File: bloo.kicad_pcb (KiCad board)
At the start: 2 copper layers, 90 x 96 mm, 97 parts, among them J5 SWD_Header, M1 M1_Conn_Alt, M2 M2_Conn_Alt, Q0 TEFT4300, Q1 TEFT4300, Q10 Q_NMOS_GSD, Q11 Q_NMOS_GSD, Q12 Q_NMOS_GSD, Q2 TEFT4300, Q3 TEFT4300, Q9 Q_NMOS_GSD, SW1 SW, SW2 SW, SW3 SW, U1 YAAJ_BluePill_SWD_Breakout, U2 L293D, U3 LM1085-5.0, U4 NCP161ASN330T1G, U5 BC832, Y1 ABS07-32.768KHZ-T

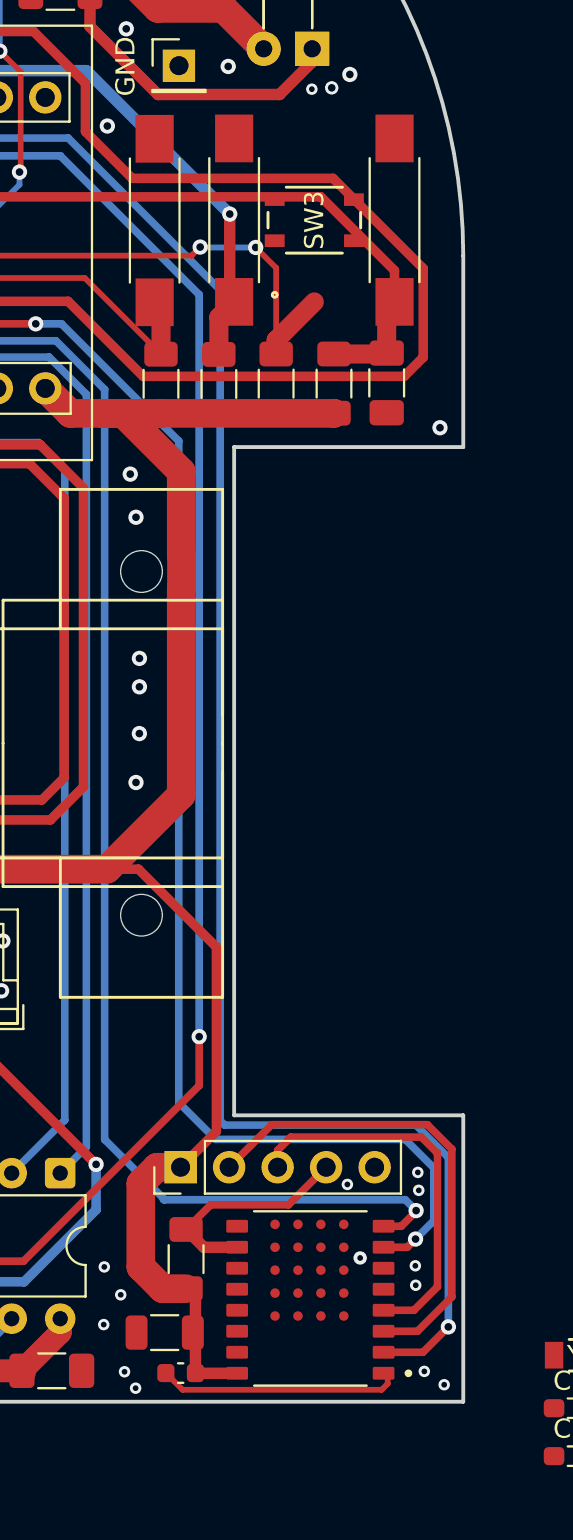
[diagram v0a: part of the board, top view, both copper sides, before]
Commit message: updated buttons in pcb
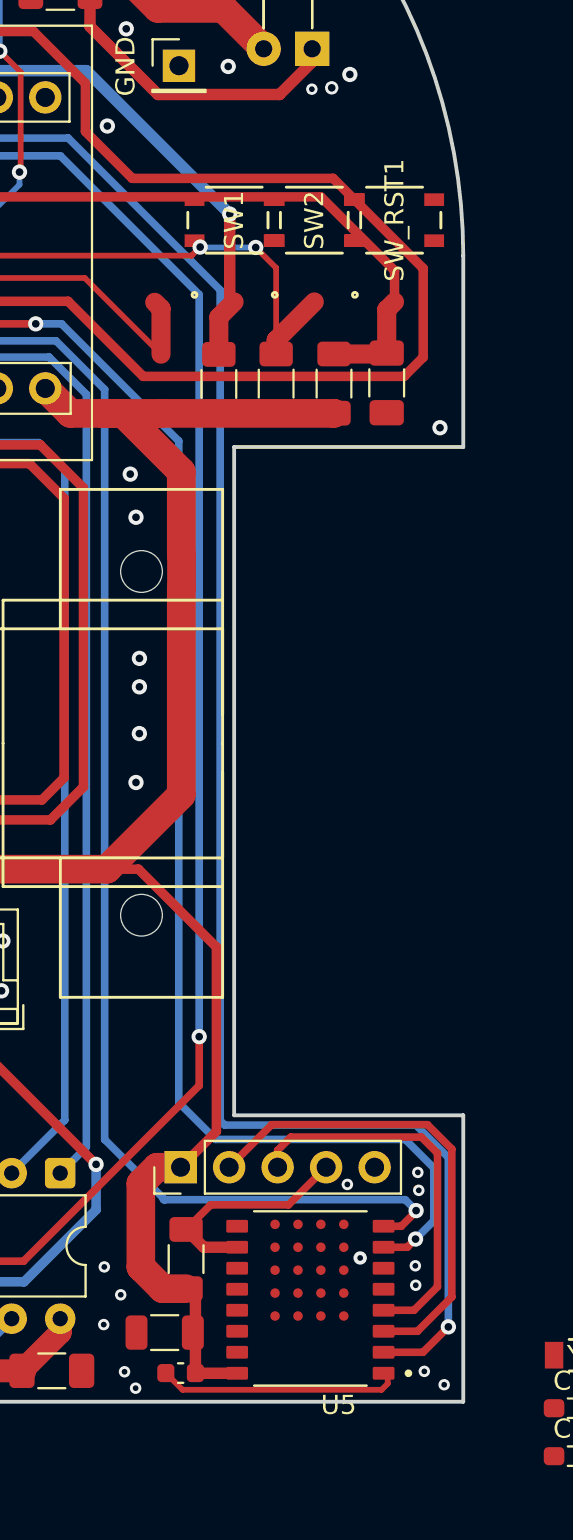
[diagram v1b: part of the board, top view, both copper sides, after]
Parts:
- removed R11: 47K, Resistor_SMD:R_1206_3216Metric_Pad1.30x1.75mm_HandSolder
- removed the SW1 at (283.3, 73.2)
- SW1: renamed from SW2; footprint Button_Switch_SMD:SW_SPST_REED_CT05-XXXX-G1 -> MM_Library:SW4_SKRPABE010_ALPS
- SW_RST1: footprint Button_Switch_SMD:SW_SPST_REED_CT05-XXXX-G1 -> MM_Library:SW4_SKRPABE010_ALPS
- U5: footprint custom_foot:XCVR_BC832 -> MM_Library:XCVR_BC832
- renumbered SW3 to SW2
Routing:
- net BUTTON: track 60.1 -> 26.8 mm, vias 2 -> 1
- net BLE_SPI_MISO: track 0.00 -> 33.3 mm, vias 0 -> 1

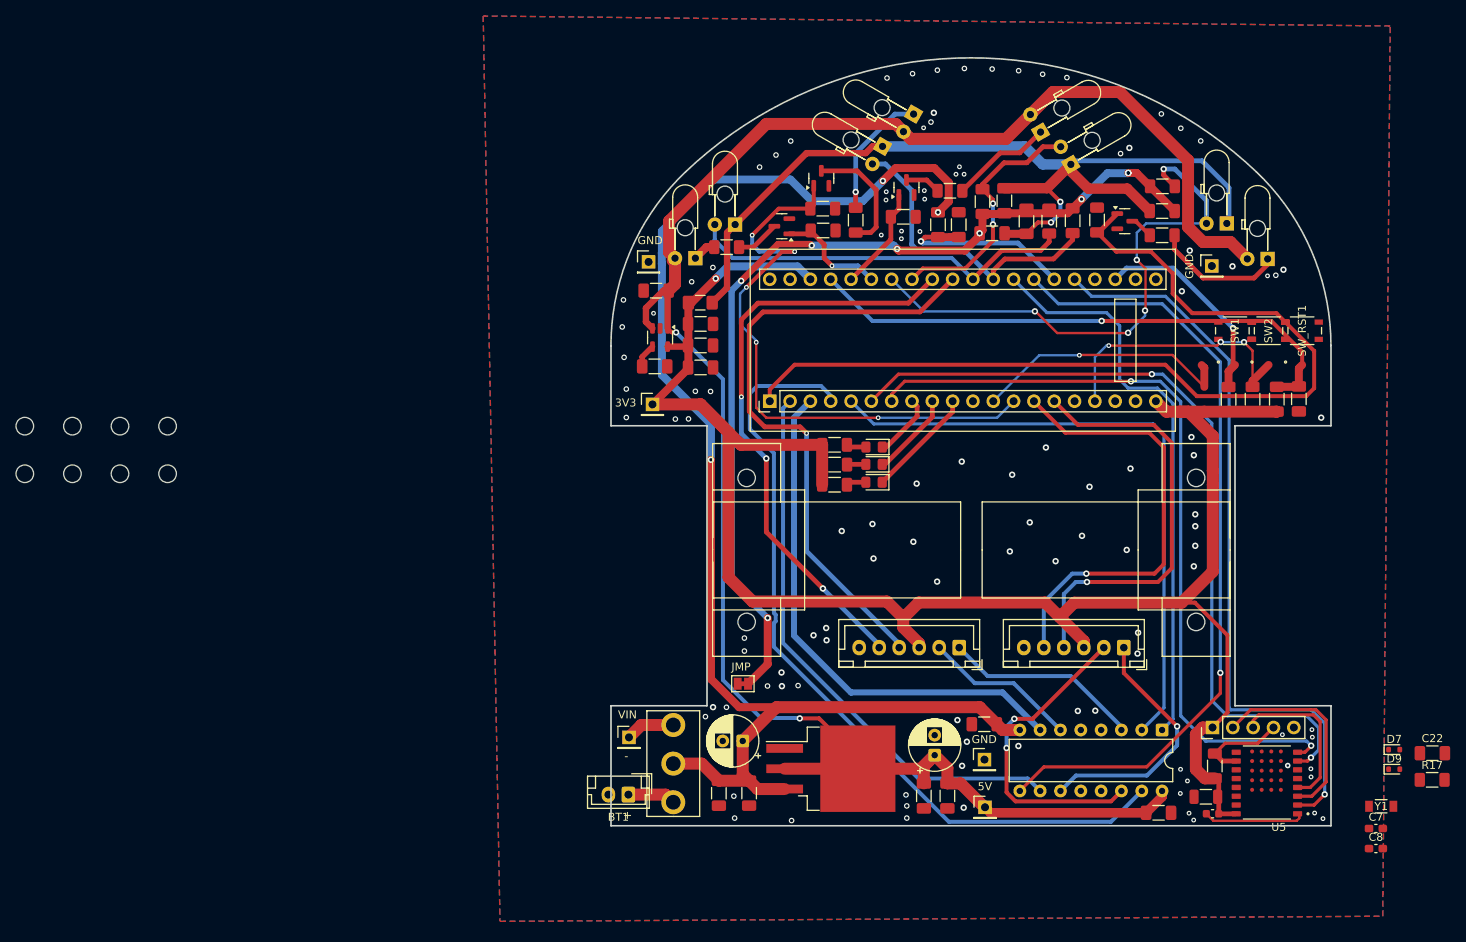
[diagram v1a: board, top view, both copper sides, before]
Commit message: started new part placement and routing
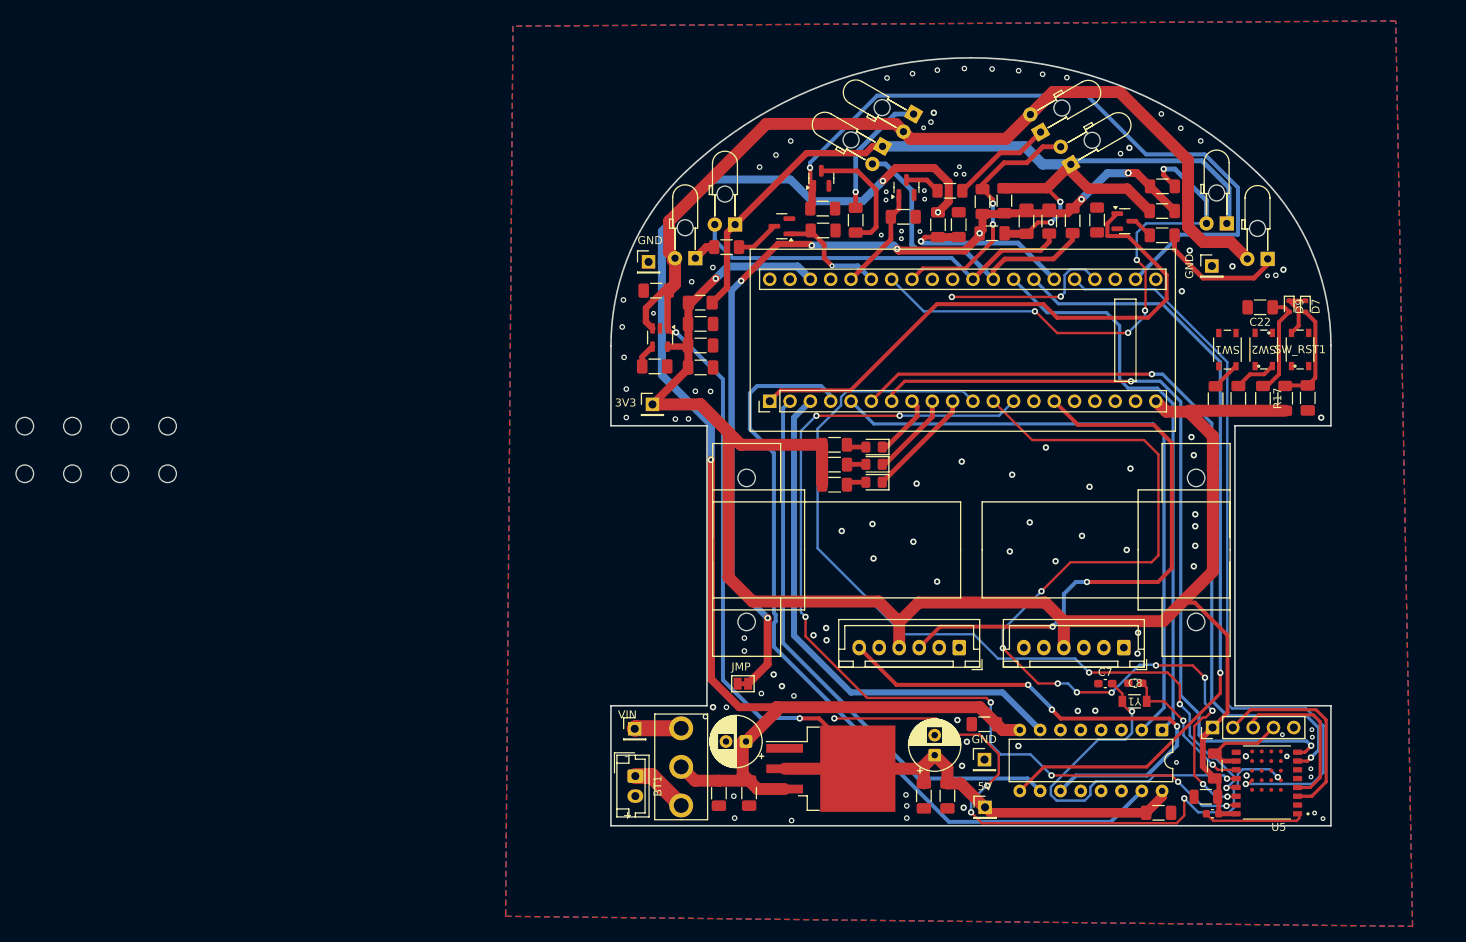
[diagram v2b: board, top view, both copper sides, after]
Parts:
- moved C22 59.8 mm to (290.6, 70.3), turned to 180 degrees
- moved D9 59.3 mm to (294.3, 70.2), turned to -90 degrees
- moved D7 56.5 mm to (296.3, 70.2), turned to -90 degrees
- moved R17 52.2 mm to (291.0, 81.7), turned to -90 degrees
- moved C7 38.4 mm to (271.3, 117.3)
- moved C8 36.5 mm to (275.0, 117.3)
- moved Y1 33.5 mm to (274.9, 119.5), turned to 180 degrees
- moved SW1 2.55 mm to (286.6, 75.6), turned to 180 degrees
- moved BT1 2.48 mm to (212.6, 128.9), turned to -90 degrees
- moved SW2 2.43 mm to (291.1, 75.6), turned to 180 degrees
- moved SW_RST1 2.36 mm to (295.6, 75.6), turned to 0 degrees
- moved R9 1.78 mm to (287.9, 81.7)
- moved R24 1.62 mm to (285.1, 81.7)
- moved TP1 1.29 mm to (212.5, 123.0)
- moved C19 1.12 mm to (296.6, 81.6), turned to 90 degrees
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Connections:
- U5 pad 13: unconnected-(U5-P02/AIN0-Pad13) -> BLE_SPI_SCK
- U5 pad 14: unconnected-(U5-P27/SCL-Pad14) -> BLE_SPI_MISO
- U5 pad 15: unconnected-(U5-P26/SDA-Pad15) -> BLE_SPI_MOSI
- U5 pad A5: BLE_SPI_SCK -> unconnected-(U5-P08-PadA5)
- U5 pad C5: BLE_SPI_MISO -> unconnected-(U5-P09-PadC5)
- U5 pad D5: BLE_SPI_MOSI -> unconnected-(U5-P10-PadD5)
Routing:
- net BLE_SPI_MOSI: track 0.00 -> 119.8 mm, vias 0 -> 7
- net BLE_SPI_SCK: track 0.00 -> 107.3 mm, vias 0 -> 3
- net BLE_LED: track 0.00 -> 99.8 mm, vias 0 -> 7
- net M1_ENC_A: track 78.4 -> 0.00 mm, vias 1 -> 0
- net BLE_SPI_MISO: track 33.3 -> 111.4 mm, vias 1 -> 10
- net M1_ENC_B: track 74.3 -> 0.00 mm, vias 3 -> 0
- net RST: track 70.0 -> 13.0 mm, vias 1 -> 0
- net M2_ENC_B: track 55.9 -> 0.00 mm, vias 1 -> 0
- net Net-(U5-P01/XL2): track 0.00 -> 46.8 mm, vias 0 -> 2
- net EMIT_1: track 115.7 -> 72.1 mm
- net M2_OUT_2: track 39.8 -> 0.00 mm, vias 2 -> 0
- net M2_OUT_1: track 31.9 -> 63.2 mm, vias 1 -> 3
- net BUTTON_2: track 34.5 -> 5.28 mm, vias 3 -> 0
- net M1_OUT_1: track 24.8 -> 0.00 mm
- net BUTTON: track 26.8 -> 3.59 mm, vias 1 -> 0
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
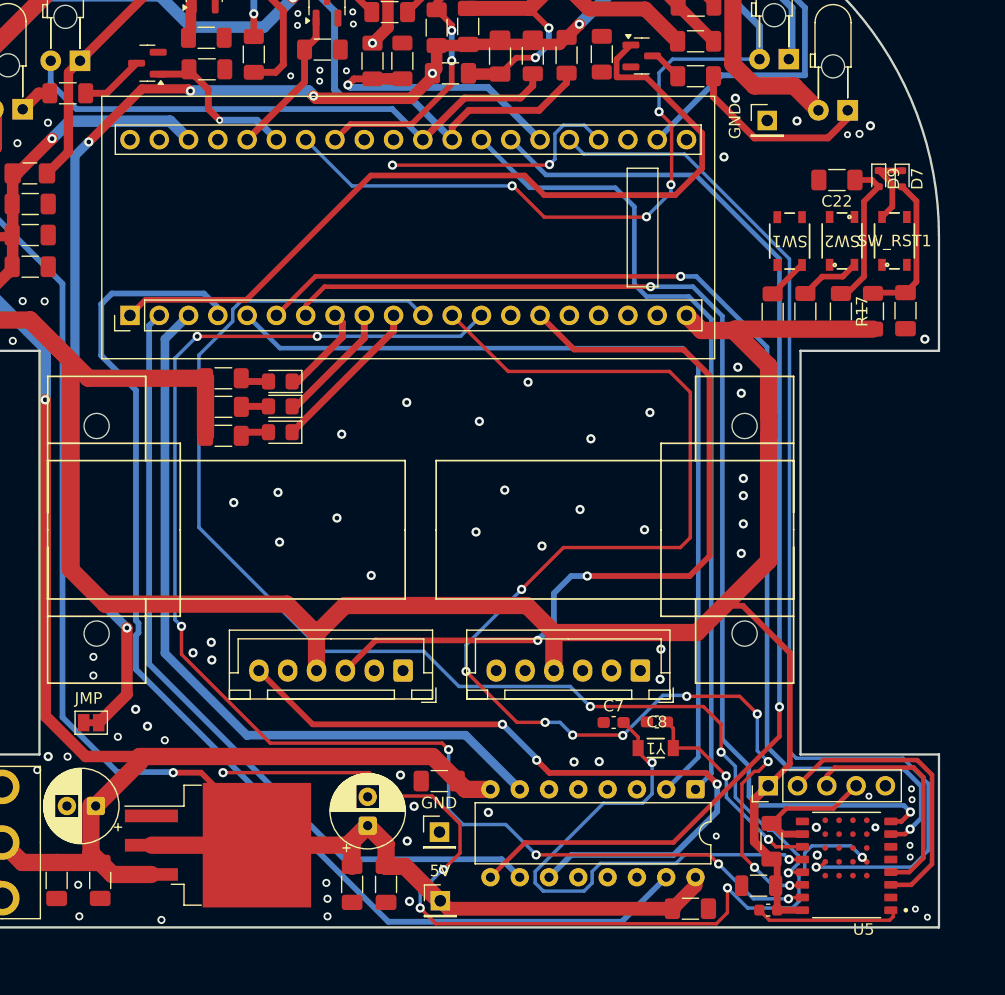
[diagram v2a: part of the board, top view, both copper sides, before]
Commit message: finished rerouting + no more DRC errors
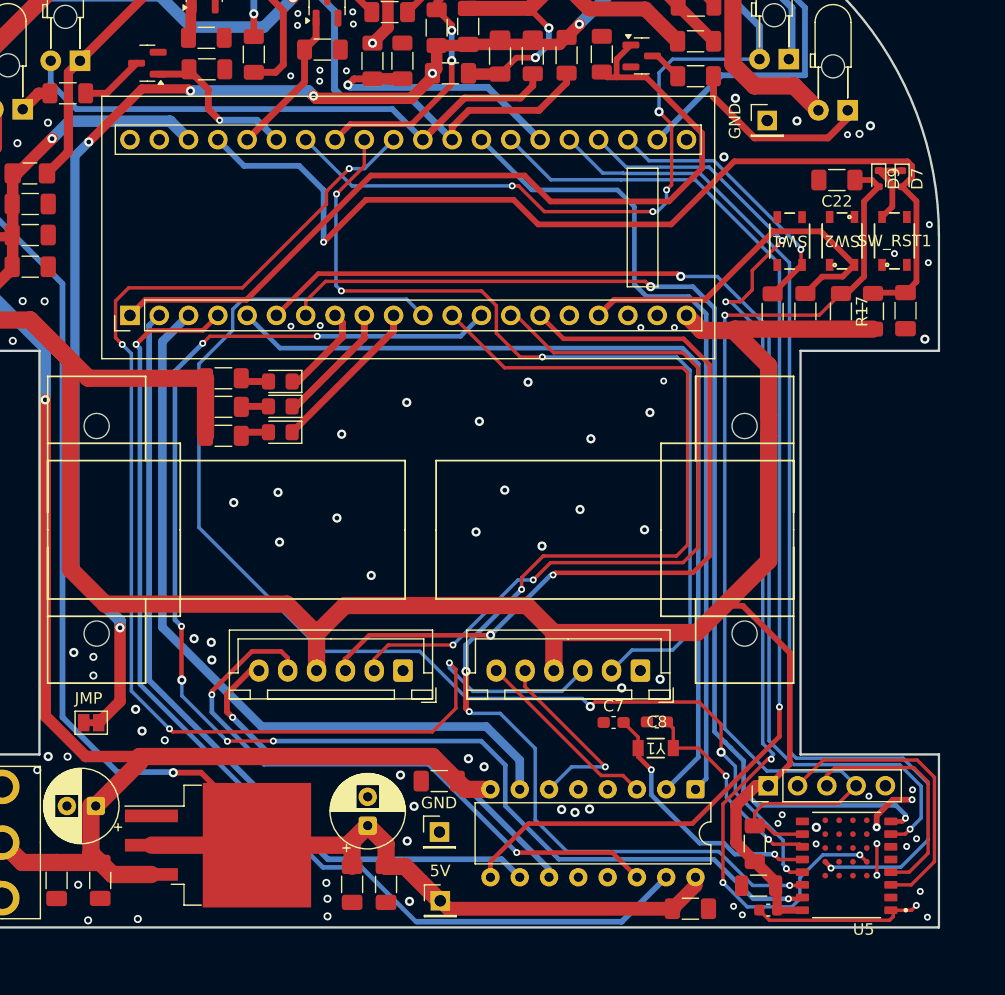
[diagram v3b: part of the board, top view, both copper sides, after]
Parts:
- moved R10 1.47 mm to (283.5, 127.8)
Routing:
- net M1_ENC_A: track 0.00 -> 113.1 mm, vias 0 -> 4
- net M1_ENC_B: track 0.00 -> 79.7 mm, vias 0 -> 3
- net RST: track 13.0 -> 86.5 mm, vias 0 -> 1
- net M2_ENC_B: track 0.00 -> 66.8 mm, vias 0 -> 2
- net BT_RESET: track 25.0 -> 88.7 mm, vias 0 -> 1
- net M2_OUT_2: track 0.00 -> 53.9 mm, vias 0 -> 2
- net BUTTON_2: track 5.28 -> 31.7 mm
- net M2_OUT_1: track 63.2 -> 39.4 mm, vias 3 -> 1
- net Net-(U5-P01/XL2): track 46.8 -> 23.1 mm
- net BUTTON: track 3.59 -> 23.9 mm, vias 0 -> 1
- net M1_OUT_2: track 0.00 -> 16.9 mm, vias 0 -> 1
- net M1_OUT_1: track 0.00 -> 16.5 mm
- net GND: track 12.8 -> 22.6 mm, vias 109 -> 119
- net M2_BACK: track 101.4 -> 93.5 mm, vias 0 -> 1
- net BLE_SPI_MISO: track 111.4 -> 105.5 mm, vias 10 -> 4
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
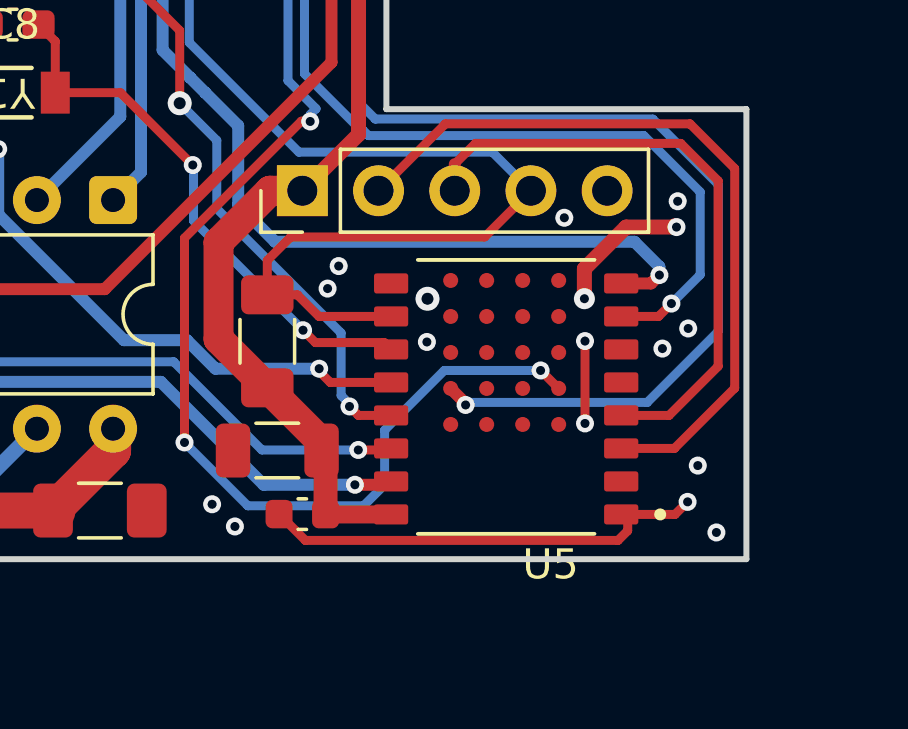
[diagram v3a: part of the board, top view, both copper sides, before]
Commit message: rerouted LED/State to edge pins on BLE
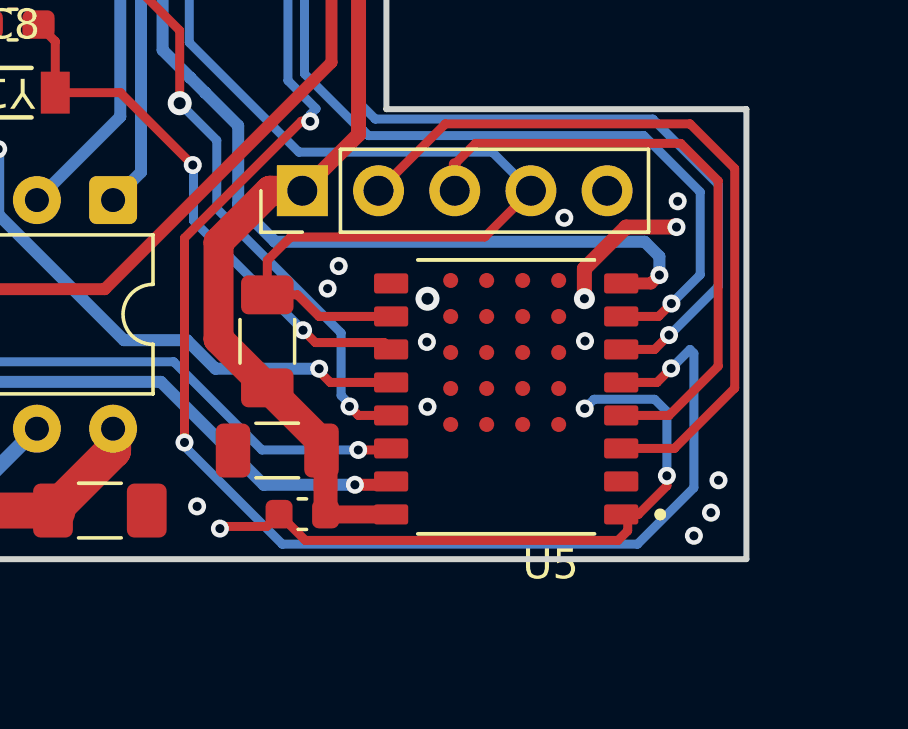
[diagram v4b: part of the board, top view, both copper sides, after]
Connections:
- U5 pad 5: unconnected-(U5-P18/LED-Pad5) -> BLE_LED
- U5 pad 6: unconnected-(U5-P13/BUTTON-Pad6) -> BLE_STATE
- U5 pad A2: BLE_LED -> unconnected-(U5-P17-PadA2)
- U5 pad D2: BLE_STATE -> unconnected-(U5-P19-PadD2)
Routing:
- net BLE_LED: track 98.5 -> 108.6 mm
- net BLE_STATE: track 94.1 -> 86.5 mm
- net GND: track 22.6 -> 27.7 mm, vias 119 -> 118
- net (no net): vias 0 -> 1
